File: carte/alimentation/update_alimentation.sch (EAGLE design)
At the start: 26 parts, among them IC1 LM2596T, K1 RP811005, T1 2N2222, X10 22-23-2021, X11 22-23-2021, X9 22-23-2021

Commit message: MAJ layout eagle
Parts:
- added C2, C5: (no value), resistor:C-EUC0603
- added D2: 1N5624, diode:1N5624
- added IC2: LM2596T, national-semiconductor:LM2596T
- added J1, J2, J3: (no value), con-amp:MTA04-100
- added L2: (no value), inductor-neosid:SM-L15A
- C3: value (none) -> 1000u
- R2: value (none) -> 12K
- R3: value (none) -> 330
- R4: value (none) -> 18K
- R7: value (none) -> 220
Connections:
- net 5V1A renamed +5V_3A
- removed net N$7: C4.1, IC1.VIN
- new net +5V: C2.1, IC2.FB, L2.2
- new net BOBINE: D4.A, K11.2, R3.2, R7.2
- new net N$2: D4.C, K11.1, K12.P, R1.1, R4.1, X15-2.KL
- net GND: now also C2.2, C5.2, D2.A, IC2.!ON!/OFF, IC2.GND, J1.4, J2.4, J3.4; no longer C4.2, IC1.!ON!/OFF, IC1.GND
- net N$11: now also C4.1, IC1.VIN
- net N$22: no longer R3.2, R7.2
- net N$5: now also R1.2, R6.A; no longer D4.C, K11.1, K12.P, R4.1, X15-2.KL
- net N$6: now also C4.2, C5.1, IC1.!ON!/OFF, IC1.GND, IC2.VIN; no longer K11.2, R1.1
- net N$9: now also D2.C, IC2.OUT, L2.1; no longer D4.A, R1.2, R6.A
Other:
- moved on the sheet: C1, C3, C4, D1, D3, D4, IC1, K1, L1, LED1, R1, R2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

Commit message: MAJ layout eagle
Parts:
- removed D3: BZX90, diode:BZX90
- removed D4: 1N4004, diode:1N4004
- removed K1: RP811005, relay:RP811005
- removed LED1: (no value), eagle-ltspice:LED_E
- removed R1: (no value), resistor:R-EU_R0805
- removed R2: 12K, resistor:R-EU_R0805
- removed R3: 330, resistor:R-EU_R0805
- removed R4: 18K, resistor:R-EU_R0805
- removed R6: (no value), pot:TRIM_EU-3223G
- removed R7: 220, resistor:R-EU_R0805
- removed T1: 2N2222, transistor:2N2222
- removed VR1: (no value), v-reg:TL431CLP
- added D5: 1N4004, diode:1N4004
- added IC3: DSPIC33FJ128MC804-PT, microchip-dspic33fjxxmc:DSPIC33FJ128MC804-PT
- added K2: RP811005, relay:RP811005
- added LED2: (no value), eagle-ltspice:LED_E
- added R5: 220, resistor:R-EU_R0805
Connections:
- removed net BOBINE: D4.A, K11.2, R3.2, R7.2
- removed net N$10: D3.A, T1.B
- removed net N$14: LED1.A, R7.1
- removed net N$15: R6.S, VR1.R
- removed net N$2: D4.C, K11.1, K12.P, R1.1, R4.1, X15-2.KL
- removed net N$21: LED1.C, R3.1, T1.C
- removed net N$22: R2.1, R4.2, VR1.C
- removed net N$5: R1.2, R6.A
- removed net N$8: D3.C, R2.2
- new net N$16: D5.C, K21.1
- new net N$7: LED2.A, R5.2
- new net RB0: D5.A, IC3.PGED1/AN2/C2IN-/RP0/CN4/RB0, K21.2
- new net RB1: IC3.PGEC1/AN3/C2IN+/RP1/CN5/RB1, LED2.C, R5.1
- net GND: no longer R6.E, T1.E, VR1.A
- net N$11: now also X15-2.KL; no longer K12.O
- net N$13: now also C5.1, IC2.VIN, K22.O
- net N$6: now also K22.P; no longer C5.1, IC2.VIN
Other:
- moved on the sheet: C1, C2, C3, C4, C5, D1, D2, IC1, IC2, L1, L2, X1-1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

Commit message: MAJ layout + création lib EAGLE
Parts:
- removed IC3: DSPIC33FJ128MC804-PT, microchip-dspic33fjxxmc:DSPIC33FJ128MC804-PT
- added C10: 1u, SmartPrj:C-EU0603-RND
- added C11, C12: 33pf, LibPerso:C-EUC0603
- added C13, C14, C15: 100n, LibPerso:C-EUC0603
- added C6, C8: 100n, SmartPrj:C-EU0603-RND
- added C7, C9: 100n, SmartPrj:C-EUC0603K
- added IC4: DSPIC33FJ128MC804PT, microchip-dspic33:DSPIC33FJ128MC804PT
- added J4: RJ11-2L-B, LibPerso:RJ11-2L-B
- added J5, J6: (no value), LibPerso:520249-2
- added ON: GREEN, led:LEDCHIP-LED0805
- added PAD1, PAD10, PAD11, PAD12, PAD13, PAD14, PAD15, PAD16, PAD17, PAD18, PAD2, PAD3, PAD4, PAD5, PAD6, PAD7, PAD8, PAD9: (no value), wirepad:1,6/0,9
- added PC2: 47u, rcl:CPOL-EUD
- added Q1: (no value), crystal:CRYSTALSM49
- added R1, R6: 1k, LibPerso:R-EU_R0805
- added R2, R4: 10k, LibPerso:R-EU_R0805
- added R3: 4.7k, LibPerso:R-EU_R0805
- added RESET: TS42031-160R-TR-7260, SmartPrj:TS42
- added SL1: (no value), con-amp-quick:M02
- added SL2: (no value), con-amp-quick:M04
- added U$1: MCP2551-I/SN, LibPerso:MCP2551-I/SN
- added U2: LP2985-33DBVR, SmartPrj:LP2985-XXDBVR33
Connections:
- new net +3V3: C10.2, C13.1, C14.1, C15.1, IC4.AVDD, IC4.VDD, IC4.VDD@2, J4.2, PAD10.P, PAD7.P, PAD8.P, PAD9.P, R4.1, U2.OUT
- new net AN0/RA0: IC4.AN0/VREF+/CN2/RA0, PAD1.P
- new net AN1/RA1: IC4.AN1/VREF-/CN3/RA1, PAD2.P
- new net CANH: J5.2, J6.2, U$1.CANH
- new net CANL: J5.3, J6.3, U$1.CANL
- new net CAN_RX: IC4.RP19/CN28/PMBE/RC3*, U$1.RXD
- new net CAN_TX: IC4.SOSCI/RP4/CN1/RB4, R3.1, U$1.TXD
- new net INT0/RP7/RB7: IC4.INT0/RP7/CN23/PMD5/RB7*
- new net N$10: IC4.SOSCO/T1CK/CN0/RA4
- new net N$2: ON.A, R1.1, R6.1
- new net N$5: C7.1, IC4.VCAP/VDDCORE
- new net N$8: R2.2, U$1.RS
- new net OSC1: C11.1, IC4.OSC1/CLKI/CN30/RA2, Q1.1
- new net OSC2: C12.1, IC4.OSC2/CLKO/CN29/RA3, Q1.2
- new net PGC: IC4.PGEC1/AN3/C2IN+/RP1/CN5/RB1, J4.5, PAD6.P
- new net PGD: IC4.PGED1/AN2/C2IN-/RP0/CN4/RB0, J4.4, PAD5.P
- new net PWM1H1/RP14/RB14: IC4.PWM1H1/DAC1LP/RTCC/RP14/CN12/PMWR/RB14
- new net PWM1H2/RP12/RB12: IC4.PWM1H2/DAC1RP/RP12/CN14/PMD0/RB12
- new net PWM1H3/RP10/RB10: IC4.PGED2/EMCD2/PWM1H3/RP10/CN16/PMD2/RB10*
- new net PWM1L1/RP15/RB15: IC4.PWM1L1/DAC1LN/RP15/CN11/PMCS1/RB15
- new net PWM1L2/RP13/RB13: IC4.PWM1L2/DAC1RN/RP13/CN13/PMRD/RB13
- new net PWM1L3/RP11/RB11: IC4.PGEC2/PWM1L3/RP11/CN15/PMD1/RB11*
- new net PWM2H1/RP22: IC4.PWM2H1/RP22/CN18/PMA1/RC6*
- new net PWM2L1/RP23/RC7: IC4.PWM2L1/RP23/CN17/PMA0/RC7*
- new net RESET: IC4._MCLR*, J4.1, R4.2, RESET.1, RESET.2
- new net RP16/RC0/AN6: IC4.AN6/DAC1RM/RP16/CN8/RC0
- new net RP17/RC1/AN7: IC4.AN7/DAC1LM/RP17/CN9/RC1
- new net RP2/RB2/AN4: IC4.AN4/C1IN-/RP2/CN6/RB2, PAD3.P
- new net RP20/TX/SDO: IC4.RP20/CN25/PMA4/RC4*, SL2.3
- new net RP21/RC5/RX/SS: IC4.RP21/CN26/PMA3/RC5*, SL2.2
- new net RP24/RC8: IC4.RP24/CN20/PMA5/RC8*
- new net RP25/RC9: IC4.RP25/CN19/PMA6/RC9*
- new net RP3/RB3/AN5: IC4.AN5/C1IN+/RP3/CN7/RB3, PAD4.P
- new net RP5/SDI/ASDA: IC4.PGED3/ASDA1/RP5/CN27/PMD7/RB5*
- new net RP6/RB6/SCK/ASCL: IC4.PGEC3/ASCL1/RP6/CN24/PMD6/RB6*
- new net SCL/RP8: IC4.SCL1/RP8/CN22/PMD4/RB8*
- new net SDA/RP9: IC4.SDA1/RP9/CN21/PMD3/RB9*
- net +5V: now also C6.2, C8.2, C9.2, J5.1, J6.1, PAD15.P, PAD16.P, PAD17.P, PAD18.P, PC2.+, R1.2, R3.2, R6.2, SL1.2, SL2.1, U$1.VDD, U2.IN, U2.ON/!OFF
- net GND: now also C10.1, C11.2, C12.2, C13.2, C14.2, C15.2, C6.1, C7.2, C8.1, C9.1, IC4.AVSS, IC4.VSS, IC4.VSS@2, IC4.VSS@3, J4.3, J5.4, J6.4, ON.C, PAD11.P, PAD12.P, PAD13.P, PAD14.P, PC2.-, R2.1, RESET.3, RESET.4, SL1.1, SL2.4, U$1.VSS, U2.GND
- net RB0: no longer IC3.PGED1/AN2/C2IN-/RP0/CN4/RB0
- net RB1: no longer IC3.PGEC1/AN3/C2IN+/RP1/CN5/RB1
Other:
- note added: "Propulsion"
- note added: "RaspberryPi"
- note added: "dsPIC (gestion batterie)"
- moved on the sheet: X10-1, X10-2, X11-1, X11-2, X12-1, X12-2, X9-1, X9-2

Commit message: MAJ eagle
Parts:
- added IC3: LM2678T-12, national-semiconductor:LM2596T
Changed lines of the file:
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@@
 <part name="PAD17" library="wirepad" deviceset="1,6/0,9" device=""/>
 <part name="PAD18" library="wirepad" deviceset="1,6/0,9" device=""/>
+<part name="IC3" library="national-semiconductor" deviceset="LM2596" device="T" value="LM2678T-12"/>
 </parts>
 <sheets>
@@
 <instance part="PAD17" gate="1" x="477.52" y="-25.4"/>
 <instance part="PAD18" gate="1" x="477.52" y="-30.48"/>
+<instance part="IC3" gate="G$1" x="160.02" y="20.32"/>
 </instances>
 <busses>

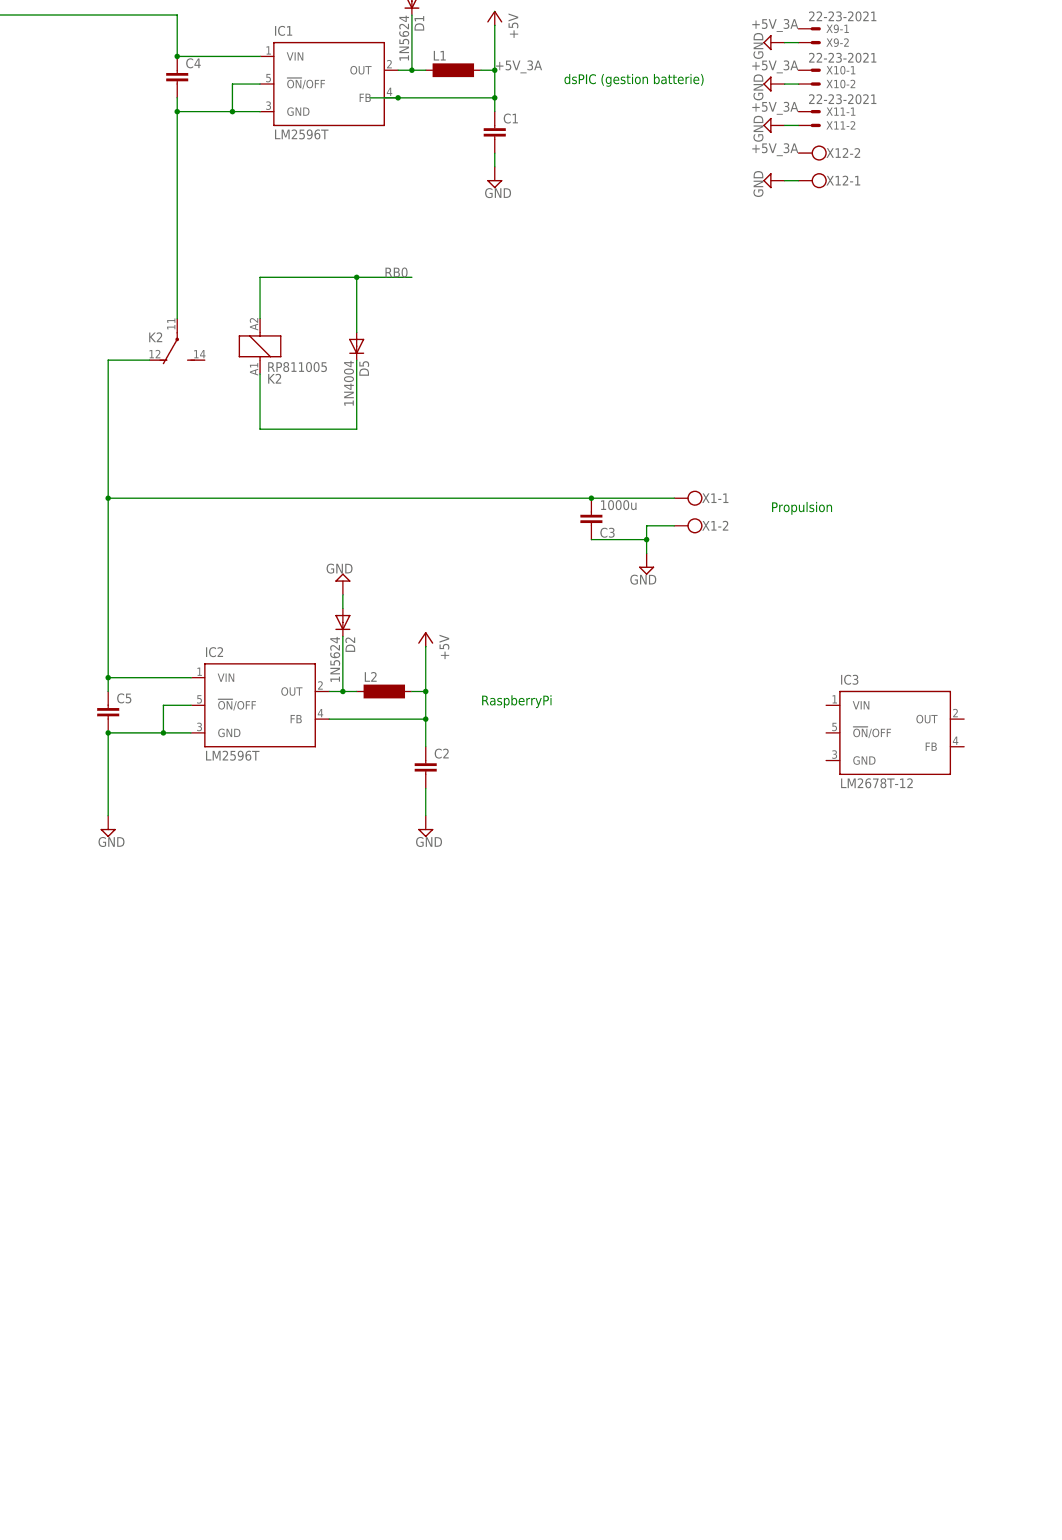
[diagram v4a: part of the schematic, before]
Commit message: MAJ layout + choix composants du LM2678
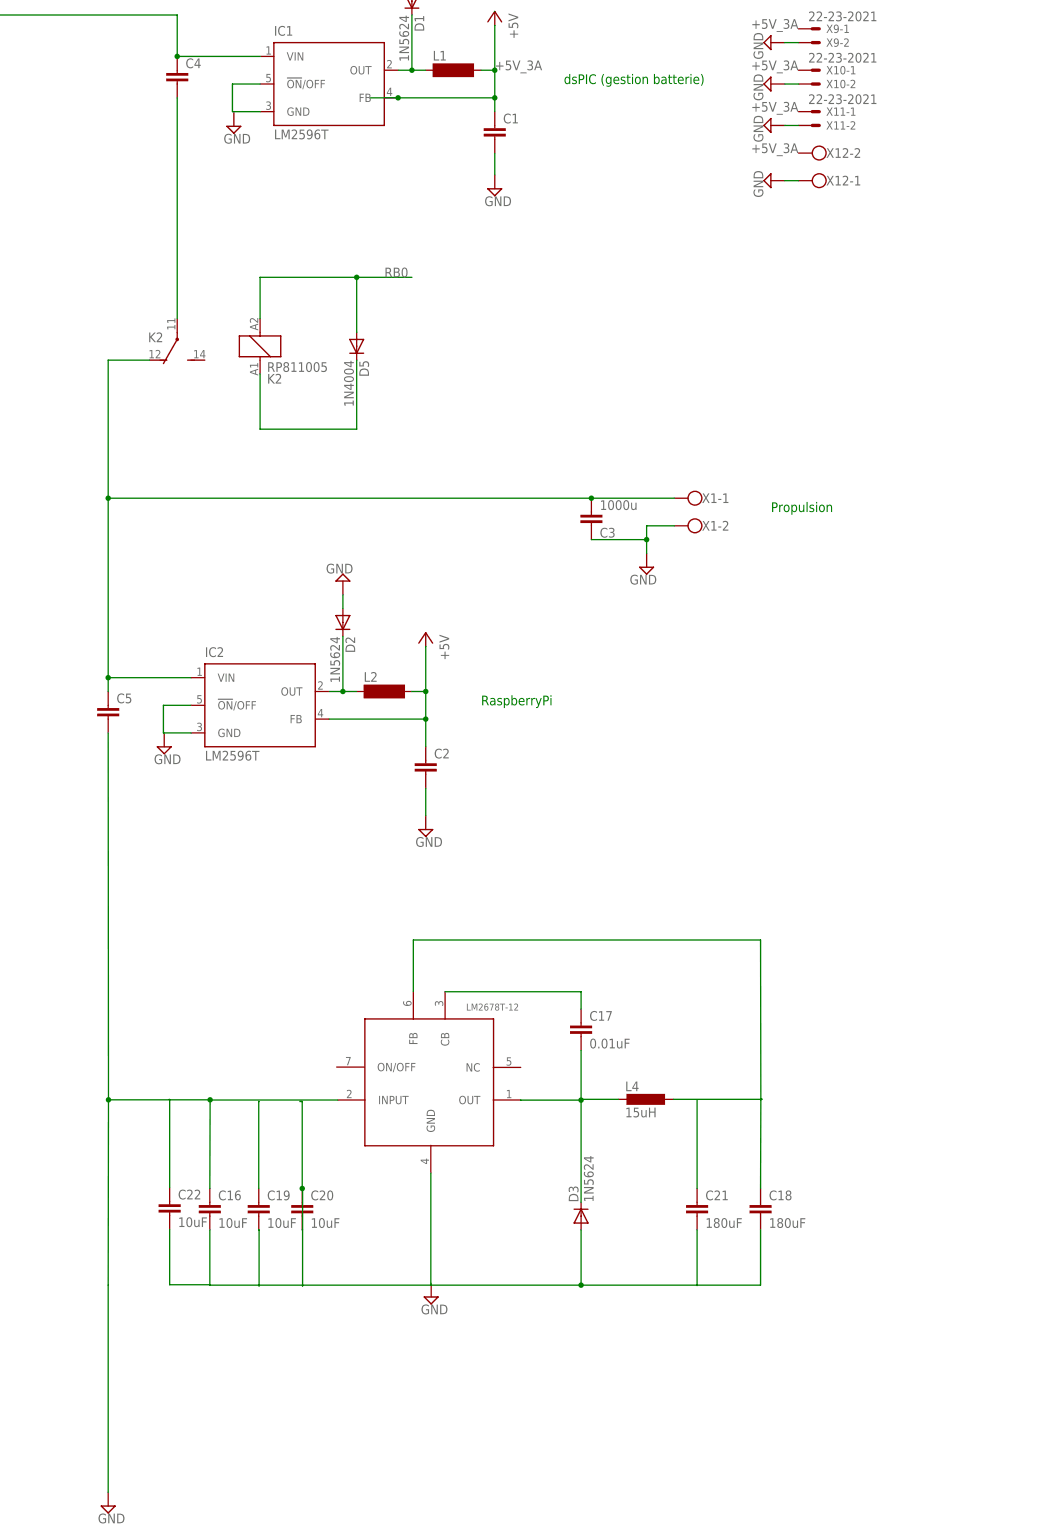
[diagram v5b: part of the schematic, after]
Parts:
- removed IC3: LM2678T-12, national-semiconductor:LM2596T
- added C16, C19, C20, C22: 10uF, resistor:C-EUC0603
- added C17: 0.01uF, resistor:C-EUC0603
- added C18, C21: 180uF, resistor:C-EUC0603
- added D3: 1N5624, diode:1N5624
- added L4: 15uH, inductor-coilcraft:DO3316P
- added LM2678T-12: (no value), Robot_MT:LM2678
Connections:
- new net N$14: C18.1, LM2678T-12.FB
- new net N$15: C17.1, LM2678T-12.CB
- new net N$17: C17.2, D3.C, LM2678T-12.OUT
- new net N$18: L4.1
- new net N$19: L4.2
- new net N$20: C21.1
- new net N$21: C21.2
- new net N$22: C19.1
- new net N$23: IC2.!ON!/OFF, IC2.GND
- new net N$24: C22.1
- new net N$25: C22.2
- new net N$26: C16.2, C18.2, D3.A, LM2678T-12.GND
- new net N$27: IC1.!ON!/OFF, IC1.GND
- new net N$28: C19.2
- new net N$29: C20.1, C20.2
- net GND: now also C16.1, LM2678T-12.INPUT; no longer IC2.!ON!/OFF, IC2.GND
- net N$6: no longer IC1.!ON!/OFF, IC1.GND

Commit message: Ajout attributes eagle
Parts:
- LM2678T-12: OC_FARNELL (none) -> 9778357
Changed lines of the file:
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@@
 <setting verticaltext="up"/>
 </settings>
-<grid distance="0.5" unitdist="mm" unit="mm" style="lines" multiple="1" display="no" altdistance="0.01" altunitdist="inch" altunit="inch"/>
+<grid distance="0.1" unitdist="inch" unit="inch" style="lines" multiple="1" display="no" altdistance="0.01" altunitdist="inch" altunit="inch"/>
 <layers>
 <layer number="1" name="Top" color="4" fill="1" visible="no" active="no"/>
@@
 <part name="C17" library="resistor" deviceset="C-EU" device="C0603" value="0.01uF"/>
 <part name="C18" library="resistor" deviceset="C-EU" device="C0603" value="180uF"/>
-<part name="LM2678T-12" library="Robot_MT" deviceset="LM2678" device=""/>
+<part name="LM2678T-12" library="Robot_MT" deviceset="LM2678" device="">
+<attribute name="OC_FARNELL" value="9778357"/>
+</part>
 <part name="L4" library="inductor-coilcraft" library_urn="urn:adsk.eagle:library:240" deviceset="DO3316P" device="" package3d_urn="urn:adsk.eagle:package:14500/1" value="15uH"/>
 <part name="C21" library="resistor" deviceset="C-EU" device="C0603" value="180uF"/>
@@
 <instance part="C17" gate="G$1" x="102.24" y="-33.02"/>
 <instance part="C18" gate="G$1" x="135.26" y="-66.04"/>
-<instance part="LM2678T-12" gate="G$1" x="74.3" y="-45.72"/>
+<instance part="LM2678T-12" gate="G$1" x="74.3" y="-45.72">
+<attribute name="OC_FARNELL" x="74.3" y="-45.72" size="1.778" layer="96" display="off"/>
+</instance>
 <instance part="L4" gate="G$1" x="114.13863125" y="-47.096678125"/>
 <instance part="C21" gate="G$1" x="123.582846875" y="-66.039996875"/>
